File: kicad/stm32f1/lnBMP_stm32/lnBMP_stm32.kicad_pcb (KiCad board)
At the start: 2 copper layers, 52.6 x 33 mm, 32 parts, among them J1 BMP Debug1, J2 BMP Debug2, J3 Debug port, J4 USB_OTG, U1 STM32F103CBTx, U2 LM1117-3.3, Y1 Crystal, x2 PinSocket_1x03_P1.00mm_Vertic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

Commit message: kicad : Update ch32 and stm32 pcbs
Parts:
- added DFU1: SW_DIP_x01, Button_Switch_SMD:SW_SPST_CK_RS282G05A3, F.Cu at (117.0, 94.0)
- moved J3 10.00 mm to (142.5, 81.2), turned to 90 degrees
- moved C8 0.70 mm to (149.1, 71.3)
- moved RST1 0.30 mm to (120.1, 69.6)
- moved ? 0.23 mm to (121.5, 91.4)
- moved PA4567 0.20 mm to (128.6, 96.7)
- renumbered x to ?
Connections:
- C1 pad 1: Net-(U1-NRST) -> NRST
- J3 pad 1: GND -> NRST
- J3 pad 2: SWDCLK -> UART_TX
- J3 pad 4: UART_TX -> SWDCLK
- J3 pad 5: NRESET -> GND
- R2 pad 2: Net-(U1-NRST) -> NRST
- RST1 pad 1: Net-(U1-NRST) -> NRST
- U1 pad 7: Net-(U1-NRST) -> NRST
- x2 pad 2: IN_FORCE_DFU -> unconnected-(U1-PB13-Pad26)
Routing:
- net NRST: track 0.00 -> 70.8 mm, vias 0 -> 5
- net Net-(U1-NRST): track 34.8 -> 0.00 mm, vias 4 -> 0
- net IN_FORCE_DFU: track 8.48 -> 34.4 mm, vias 0 -> 4
- net +3.3V: track 120.6 -> 133.8 mm, vias 5 -> 7
- net unconnected-(U1-PB13-Pad26): track 0.00 -> 8.60 mm
- net INOUT_NRESET: track 56.1 -> 60.5 mm
- net unconnected-(U1-PA7-Pad17): track 6.91 -> 6.20 mm, vias 1 -> 0
- net OUT_UART_TX: track 32.2 -> 32.8 mm
- net unconnected-(U1-PA4-Pad14): track 6.17 -> 5.58 mm
- net OUT_UART_RX: track 28.9 -> 29.5 mm
- net unconnected-(U1-PA6-Pad16): track 6.36 -> 5.99 mm, vias 1 -> 0
- net unconnected-(U1-PA5-Pad15): track 5.85 -> 5.79 mm, vias 1 -> 0
- net GND: track 228.4 -> 228.3 mm, vias 4 -> 11
- removed copper zone on B.Cu, net GND
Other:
- board text added: "NC"
- board text added: "REVB ARM"
- board text removed: "REVB"
- board text removed: "locked"

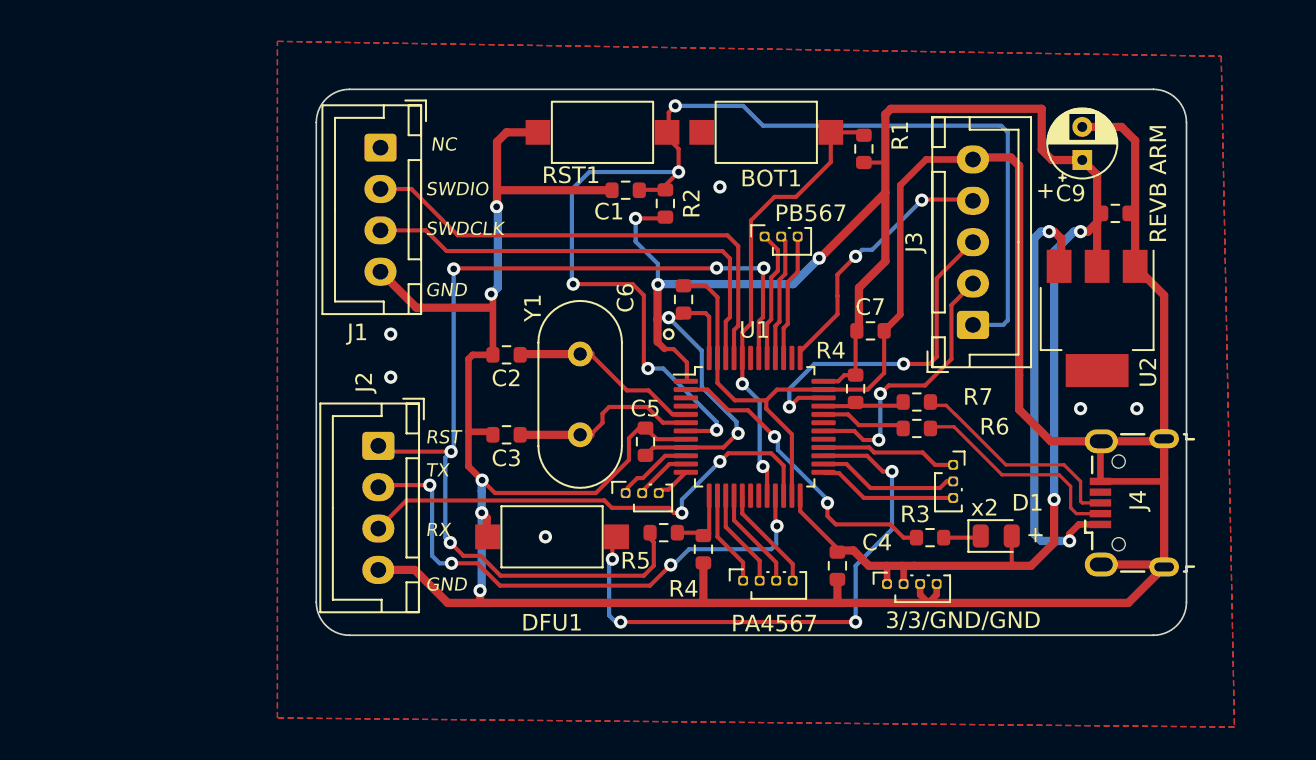
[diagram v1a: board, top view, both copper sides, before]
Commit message: cleanup a bit the text + fix the inverted BOOT signal on stm32F1
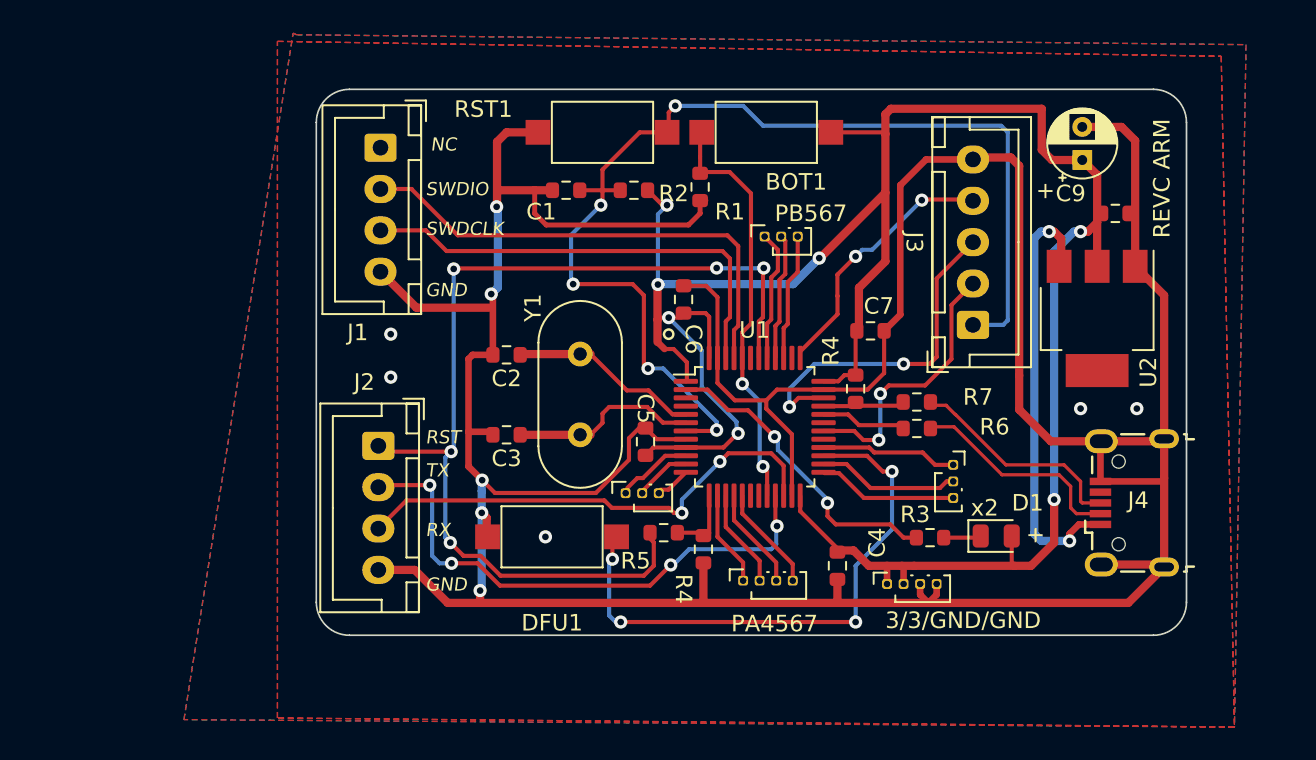
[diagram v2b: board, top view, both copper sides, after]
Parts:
- BOT1: value SW_DIP_x01 -> SW1
- C1, C4, C5, C6, C7, C9: value C_Small -> 100n
- C2, C3: value C_Small -> 10pF
- R2: value R_Small -> 10k
- R3: value R_Small -> 330
- RST1: value SW_DIP_x01 -> SW2
- moved R1 10.2 mm to (126.0, 72.9), turned to -90 degrees
- moved C1 3.60 mm to (117.9, 73.1)
- moved R2 2.06 mm to (122.0, 73.1), turned to 180 degrees
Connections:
- BOT1 pad 1: Net-(U1-BOOT0) -> +3.3V
- BOT1 pad 2: GND -> Net-(U1-BOOT0)
- R1 pad 1: +3.3V -> Net-(U1-BOOT0)
- R1 pad 2: Net-(U1-BOOT0) -> GND
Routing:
- net GND: track 228.3 -> 238.1 mm, vias 11 -> 10
- net NRST: track 70.8 -> 67.4 mm
- net +3.3V: track 133.8 -> 136.3 mm
- net Net-(U1-BOOT0): track 27.6 -> 25.2 mm
- added copper zone on B.Cu, net GND
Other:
- board text added: "REVC ARM"
- board text removed: "REVB ARM"

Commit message: stm32/gd32 : reduce rst input resistor, it acts as if a pulldown was behind
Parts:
- R5: value 10k -> 1k

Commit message: update lnArduino
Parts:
- added J5: Conn_ARM_JTAG_SWD_10, Connector_PinHeader_1.27mm:PinHeader_2x05_P1.27mm_Vertical_SMD, F.Cu at (91.0, 80.8)

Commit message: cleanup kicak / stm32
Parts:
- removed J5: Conn_ARM_JTAG_SWD_10, Connector_PinHeader_1.27mm:PinHeader_2x05_P1.27mm_Vertical_SMD
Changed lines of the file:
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@@
   (net 45 "unconnected-(U1-PC15-Pad4)")
   (net 46 "Net-(U1-PC13)")
-  (net 47 "unconnected-(J5-KEY-Pad7)")
-  (net 48 "unconnected-(J5-SWO{slash}TDO-Pad6)")
-  (net 49 "unconnected-(J5-VTref-Pad1)")
-  (net 50 "unconnected-(J5-NC{slash}TDI-Pad8)")
   (footprint "Connector_USB:USB_Micro-B_Wuerth_629105150521" (layer "F.Cu")
     (at 152.1 92 90)
@@
       (offset (xyz 0 0 0))
       (scale (xyz 1 1 1))
-      (rotate (xyz 0 0 0))
-    )
-  )
-  (footprint "Connector_PinHeader_1.27mm:PinHeader_2x05_P1.27mm_Vertical_SMD" (layer "F.Cu")
-    (at 90.95 80.76 90)
-    (descr "surface-mounted straight pin header, 2x05, 1.27mm pitch, double rows")
-    (tags "Surface mounted pin header SMD 2x05 1.27mm double row")
-    (property "Reference" "J5" (at 0 -4.235 270) (layer "F.SilkS")
-      (effects (font (size 1 1) (thickness 0.15)))
-    )
-    (property "Value" "Conn_ARM_JTAG_SWD_10" (at 0 4.235 270) (layer "F.Fab")
-      (effects (font (size 1 1) (thickness 0.15)))
-    )
-    (property "Footprint" "Connector_PinHeader_1.27mm:PinHeader_2x05_P1.27mm_Vertical_SMD" (at 0 0 90 unlocked) (layer "F.Fab") hide
-      (effects (font (size 1.27 1.27)))
-    )
-    (property "Datasheet" "http://infocenter.arm.com/help/topic/com.arm.doc.ddi0314h/DDI0314H_coresight_components_trm.pdf" (at 0 0 90 unlocked) (layer "F.Fab") hide
-      (effects (font (size 1.27 1.27)))
-    )
-    (property "Description" "Cortex Debug Connector, standard ARM Cortex-M SWD and JTAG interface" (at 0 0 90 unlocked) (layer "F.Fab") hide
-      (effects (font (size 1.27 1.27)))
-    )
-    (property ki_fp_filters "PinHeader?2x05?P1.27mm*")
-    (sheetfile "lnBMP_stm32.kicad_sch")
-    (attr smd)
-    (fp_line (start 1.765 -3.235) (end 1.765 -3.17)
-      (stroke (width 0.12) (type solid)) (layer "F.SilkS"))
-    (fp_line (start -1.765 -3.235) (end 1.765 -3.235)
-      (stroke (width 0.12) (type solid)) (layer "F.SilkS"))
-    (fp_line (start -1.765 -3.235) (end -1.765 -3.17)
-      (stroke (width 0.12) (type solid)) (layer "F.SilkS"))
-    (fp_line (start -3.09 -3.17) (end -1.765 -3.17)
-      (stroke (width 0.12) (type solid)) (layer "F.SilkS"))
-    (fp_line (start 1.765 3.17) (end 1.765 3.235)
-      (stroke (width 0.12) (type solid)) (layer "F.SilkS"))
-    (fp_line (start -1.765 3.17) (end -1.765 3.235)
-      (stroke (width 0.12) (type solid)) (layer "F.SilkS"))
-    (fp_line (start -1.765 3.235) (end 1.765 3.235)
-      (stroke (width 0.12) (type solid)) (layer "F.SilkS"))
-    (fp_line (start 4.3 -3.7) (end -4.3 -3.7)
-      (stroke (width 0.05) (type solid)) (layer "F.CrtYd"))
-    (fp_line (start -4.3 -3.7) (end -4.3 3.7)
-      (stroke (width 0.05) (type solid)) (layer "F.CrtYd"))
-    (fp_line (start 4.3 3.7) (end 4.3 -3.7)
-      (stroke (width 0.05) (type solid)) (layer "F.CrtYd"))
-    (fp_line (start -4.3 3.7) (end 4.3 3.7)
-      (stroke (width 0.05) (type solid)) (layer "F.CrtYd"))
-    (fp_line (start 1.705 -3.175) (end 1.705 3.175)
-      (stroke (width 0.1) (type solid)) (layer "F.Fab"))
-    (fp_line (start -1.27 -3.175) (end 1.705 -3.175)
-      (stroke (width 0.1) (type solid)) (layer "F.Fab"))
-    (fp_line (start 2.75 -2.74) (end 2.75 -2.34)
-      (stroke (width 0.1) (type solid)) (layer "F.Fab"))
-    (fp_line (start 1.705 -2.74) (end 2.75 -2.74)
-      (stroke (width 0.1) (type solid)) (layer "F.Fab"))
-    (fp_line (start -1.705 -2.74) (end -1.27 -3.175)
-      (stroke (width 0.1) (type solid)) (layer "F.Fab"))
-    (fp_line (start -1.705 -2.74) (end -2.75 -2.74)
-      (stroke (width 0.1) (type solid)) (layer "F.Fab"))
-    (fp_line (start -2.75 -2.74) (end -2.75 -2.34)
-      (stroke (width 0.1) (type solid)) (layer "F.Fab"))
-    (fp_line (start 2.75 -2.34) (end 1.705 -2.34)
-      (stroke (width 0.1) (type solid)) (layer "F.Fab"))
-    (fp_line (start -2.75 -2.34) (end -1.705 -2.34)
-      (stroke (width 0.1) (type solid)) (layer "F.Fab"))
-    (fp_line (start 2.75 -1.47) (end 2.75 -1.07)
-      (stroke (width 0.1) (type solid)) (layer "F.Fab"))
-    (fp_line (start 1.705 -1.47) (end 2.75 -1.47)
-      (stroke (width 0.1) (type solid)) (layer "F.Fab"))
-    (fp_line (start -1.705 -1.47) (end -2.75 -1.47)
-      (stroke (width 0.1) (type solid)) (layer "F.Fab"))
-    (fp_line (start -2.75 -1.47) (end -2.75 -1.07)
-      (stroke (width 0.1) (type solid)) (layer "F.Fab"))
-    (fp_line (start 2.75 -1.07) (end 1.705 -1.07)
-      (stroke (width 0.1) (type solid)) (layer "F.Fab"))
-    (fp_line (start -2.75 -1.07) (end -1.705 -1.07)
-      (stroke (width 0.1) (type solid)) (layer "F.Fab"))
-    (fp_line (start 2.75 -0.2) (end 2.75 0.2)
-      (stroke (width 0.1) (type solid)) (layer "F.Fab"))
-    (fp_line (start 1.705 -0.2) (end 2.75 -0.2)
-      (stroke (width 0.1) (type solid)) (layer "F.Fab"))
-    (fp_line (start -1.705 -0.2) (end -2.75 -0.2)
-      (stroke (width 0.1) (type solid)) (layer "F.Fab"))
-    (fp_line (start -2.75 -0.2) (end -2.75 0.2)
-      (stroke (width 0.1) (type solid)) (layer "F.Fab"))
-    (fp_line (start 2.75 0.2) (end 1.705 0.2)
-      (stroke (width 0.1) (type solid)) (layer "F.Fab"))
-    (fp_line (start -2.75 0.2) (end -1.705 0.2)
-      (stroke (width 0.1) (type solid)) (layer "F.Fab"))
-    (fp_line (start 2.75 1.07) (end 2.75 1.47)
-      (stroke (width 0.1) (type solid)) (layer "F.Fab"))
-    (fp_line (start 1.705 1.07) (end 2.75 1.07)
-      (stroke (width 0.1) (type solid)) (layer "F.Fab"))
-    (fp_line (start -1.705 1.07) (end -2.75 1.07)
-      (stroke (width 0.1) (type solid)) (layer "F.Fab"))
-    (fp_line (start -2.75 1.07) (end -2.75 1.47)
-      (stroke (width 0.1) (type solid)) (layer "F.Fab"))
-    (fp_line (start 2.75 1.47) (end 1.705 1.47)
-      (stroke (width 0.1) (type solid)) (layer "F.Fab"))
-    (fp_line (start -2.75 1.47) (end -1.705 1.47)
-      (stroke (width 0.1) (type solid)) (layer "F.Fab"))
-    (fp_line (start 2.75 2.34) (end 2.75 2.74)
-      (stroke (width 0.1) (type solid)) (layer "F.Fab"))
-    (fp_line (start 1.705 2.34) (end 2.75 2.34)
-      (stroke (width 0.1) (type solid)) (layer "F.Fab"))
-    (fp_line (start -1.705 2.34) (end -2.75 2.34)
-      (stroke (width 0.1) (type solid)) (layer "F.Fab"))
-    (fp_line (start -2.75 2.34) (end -2.75 2.74)
-      (stroke (width 0.1) (type solid)) (layer "F.Fab"))
-    (fp_line (start 2.75 2.74) (end 1.705 2.74)
-      (stroke (width 0.1) (type solid)) (layer "F.Fab"))
-    (fp_line (start -2.75 2.74) (end -1.705 2.74)
-      (stroke (width 0.1) (type solid)) (layer "F.Fab"))
-    (fp_line (start 1.705 3.175) (end -1.705 3.175)
-      (stroke (width 0.1) (type solid)) (layer "F.Fab"))
-    (fp_line (start -1.705 3.175) (end -1.705 -2.74)
-      (stroke (width 0.1) (type solid)) (layer "F.Fab"))
-    (fp_text user "${REFERENCE}" (at 0 0 360) (layer "F.Fab")
-      (effects (font (size 1 1) (thickness 0.15)))
-    )
-    (pad "1" smd rect (at -1.95 -2.54 90) (size 2.4 0.74) (layers "F.Cu" "F.Paste" "F.Mask")
-      (net 49 "unconnected-(J5-VTref-Pad1)") (pinfunction "VTref") (pintype "power_in")
-    )
-    (pad "2" smd rect (at 1.95 -2.54 90) (size 2.4 0.74) (layers "F.Cu" "F.Paste" "F.Mask")
-      (net 12 "OUT_SWDIO") (pinfunction "SWDIO/TMS") (pintype "bidirectional")
-    )
-    (pad "3" smd rect (at -1.95 -1.27 90) (size 2.4 0.74) (layers "F.Cu" "F.Paste" "F.Mask")
-      (net 2 "GND") (pinfunction "GND") (pintype "power_in")
-    )
-    (pad "4" smd rect (at 1.95 -1.27 90) (size 2.4 0.74) (layers "F.Cu" "F.Paste" "F.Mask")
-      (net 13 "OUT_SWDCLK") (pinfunction "SWDCLK/TCK") (pintype "output")
-    )
-    (pad "5" smd rect (at -1.95 0 90) (size 2.4 0.74) (layers "F.Cu" "F.Paste" "F.Mask")
-      (net 2 "GND") (pinfunction "GND") (pintype "passive")
-    )
-    (pad "6" smd rect (at 1.95 0 90) (size 2.4 0.74) (layers "F.Cu" "F.Paste" "F.Mask")
-      (net 48 "unconnected-(J5-SWO{slash}TDO-Pad6)") (pinfunction "SWO/TDO") (pintype "input")
-    )
-    (pad "7" smd rect (at -1.95 1.27 90) (size 2.4 0.74) (layers "F.Cu" "F.Paste" "F.Mask")
-      (net 47 "unconnected-(J5-KEY-Pad7)") (pinfunction "KEY") (pintype "no_connect")
-    )
-    (pad "8" smd rect (at 1.95 1.27 90) (size 2.4 0.74) (layers "F.Cu" "F.Paste" "F.Mask")
-      (net 50 "unconnected-(J5-NC{slash}TDI-Pad8)") (pinfunction "NC/TDI") (pintype "output")
-    )
-    (pad "9" smd rect (at -1.95 2.54 90) (size 2.4 0.74) (layers "F.Cu" "F.Paste" "F.Mask")
-      (net 2 "GND") (pinfunction "GNDDetect") (pintype "passive")
-    )
-    (pad "10" smd rect (at 1.95 2.54 90) (size 2.4 0.74) (layers "F.Cu" "F.Paste" "F.Mask")
-      (net 11 "INOUT_NRESET") (pinfunction "~{RESET}") (pintype "open_collector")
-    )
-    (model "${KICAD6_3DMODEL_DIR}/Connector_PinHeader_1.27mm.3dshapes/PinHeader_2x05_P1.27mm_Vertical_SMD.wrl"
-      (offset (xyz 0 0 0))
-      (scale (xyz 1 1 1))
